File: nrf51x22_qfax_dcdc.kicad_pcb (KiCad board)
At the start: 2 copper layers, 14.8 x 16.4 mm, 45 parts, among them U1 nrf51822-qfax, X1 Crystal, X2 XTAL SMD 3.2 x 1.5 mm

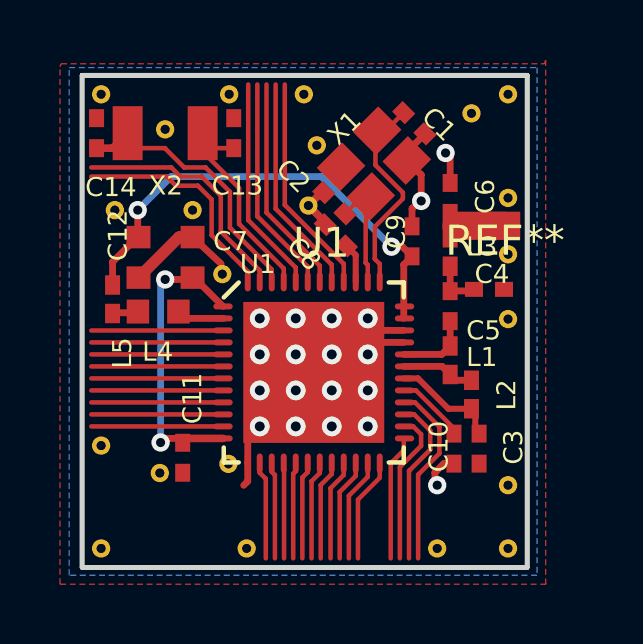
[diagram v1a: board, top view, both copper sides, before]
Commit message: missed replacing a via
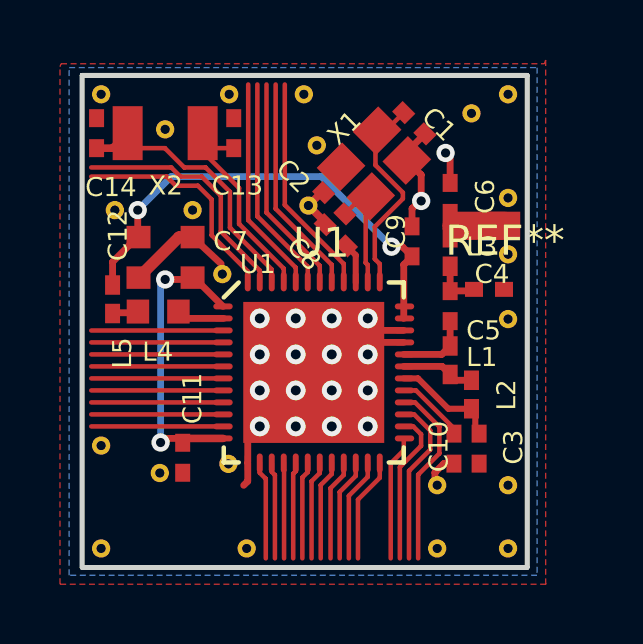
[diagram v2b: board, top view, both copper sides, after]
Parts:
- added REF**: VIA-0.6096, dcdc:VIA-0.6096, F.Cu at (88.2, -81.7)
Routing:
- net GND: vias 19 -> 18
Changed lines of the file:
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@@
 (kicad_pcb (version 4) (host pcbnew 4.0.0-stable)
   (general
-    (links 65)
+    (links 67)
     (no_connects 3)
-    (area 76.307339 -95.473821 91.295321 -78.913019)
+    (area 41.129536 -98.38002 117.176334 -76.15682)
     (thickness 1.6)
     (drawings 30)
-    (tracks 217)
+    (tracks 216)
     (zones 0)
-    (modules 45)
+    (modules 46)
     (nets 50)
   )
@@
   (layers
     (0 F.Cu signal)
-    (31 B.Cu signal hide)
+    (31 B.Cu signal)
     (32 B.Adhes user)
     (33 F.Adhes user)
@@
     )
   )
+  (module dcdc:VIA-0.6096 (layer F.Cu)
+    (at 88.22073 -81.73242)
+    (fp_text reference REF** (at 0 2.54) (layer F.SilkS) hide
+      (effects (font (size 1 1) (thickness 0.15)))
+    )
+    (fp_text value VIA-0.6096 (at 0 -2.54) (layer F.Fab) hide
+      (effects (font (size 1 1) (thickness 0.15)))
+    )
+    (pad 1 thru_hole circle (at 0 0) (size 0.6096 0.6096) (drill 0.3048) (layers *.Cu)
+      (zone_connect 2))
+  )
   (gr_line (start 76.38354 -78.98922) (end 76.38354 -95.39762) (layer Edge.Cuts) (width 0.1524))
   (gr_line (start 76.38354 -78.98922) (end 91.21912 -78.98922) (layer Edge.Cuts) (width 0.1524))
@@
   (segment (start 81.61673 -90.44313) (end 81.61673 -91.63842) (width 0.1524) (layer F.Cu) (net 2))
   (segment (start 81.61673 -90.44313) (end 83.10593 -88.95392) (width 0.1524) (layer F.Cu) (net 2))
-  (via (at 88.22073 -81.73242) (size 0.6096) (drill 0.3048) (layers F.Cu B.Cu) (net 3))
   (segment (start 88.14453 -81.88482) (end 88.14453 -82.15573) (width 0.2286) (layer F.Cu) (net 3))
   (segment (start 88.14453 -82.15573) (end 88.44042 -82.45162) (width 0.2286) (layer F.Cu) (net 3))

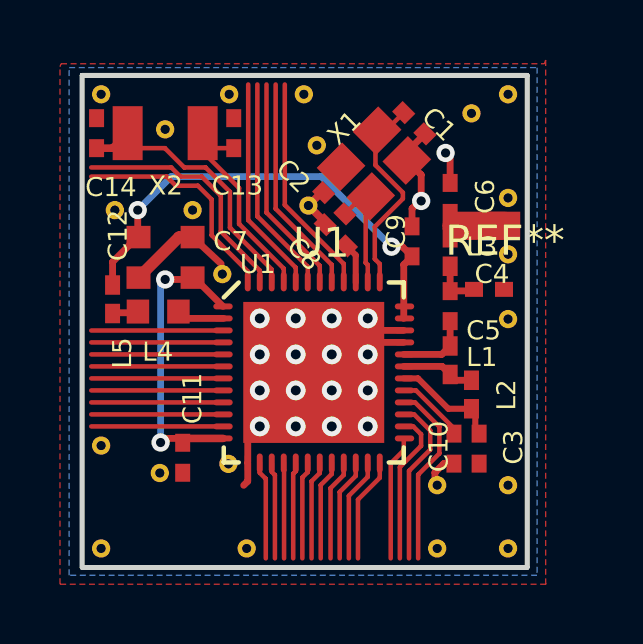
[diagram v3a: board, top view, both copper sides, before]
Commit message: add vias to footprint and swap in
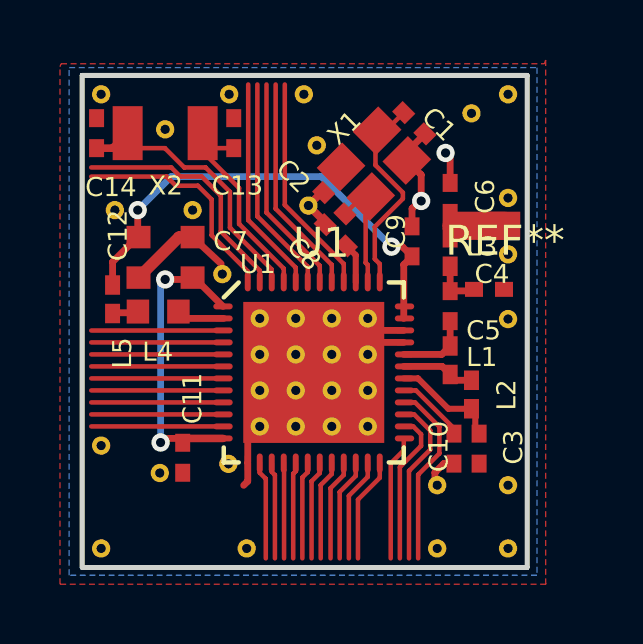
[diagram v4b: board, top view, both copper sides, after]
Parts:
- U1: footprint nrf:nrf51-qfax -> nrf:nrf51-qfax-1ep-vias
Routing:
- net GND: vias 18 -> 2

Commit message: merge library update
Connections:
- U1 pad 10: Net-(U1-Pad10) -> (no net)
- U1 pad 11: Net-(U1-Pad11) -> (no net)
- U1 pad 14: Net-(U1-Pad14) -> (no net)
- U1 pad 15: Net-(U1-Pad15) -> (no net)
- U1 pad 16: Net-(U1-Pad16) -> (no net)
- U1 pad 17: Net-(U1-Pad17) -> (no net)
- U1 pad 18: Net-(U1-Pad18) -> (no net)
- U1 pad 19: Net-(U1-Pad19) -> (no net)
- U1 pad 20: Net-(U1-Pad20) -> (no net)
- U1 pad 21: Net-(U1-Pad21) -> (no net)
- U1 pad 22: Net-(U1-Pad22) -> (no net)
- U1 pad 23: Net-(U1-Pad23) -> (no net)
- U1 pad 24: Net-(U1-Pad24) -> (no net)
- U1 pad 25: Net-(U1-Pad25) -> (no net)
- U1 pad 26: Net-(U1-Pad26) -> (no net)
- U1 pad 27: Net-(U1-Pad27) -> (no net)
- U1 pad 28: Net-(U1-Pad28) -> (no net)
- U1 pad 3: Net-(U1-Pad3) -> (no net)
- U1 pad 4: Net-(U1-Pad4) -> (no net)
- U1 pad 40: Net-(U1-Pad40) -> (no net)
- U1 pad 41: Net-(U1-Pad41) -> (no net)
- U1 pad 42: Net-(U1-Pad42) -> (no net)
- U1 pad 43: Net-(U1-Pad43) -> (no net)
- U1 pad 44: Net-(U1-Pad44) -> (no net)
- U1 pad 45: Net-(U1-Pad45) -> (no net)
- U1 pad 46: Net-(U1-Pad46) -> (no net)
- U1 pad 47: Net-(U1-Pad47) -> (no net)
- U1 pad 48: Net-(U1-Pad48) -> (no net)
- U1 pad 5: Net-(U1-Pad5) -> (no net)
- U1 pad 6: Net-(U1-Pad6) -> (no net)
- U1 pad 7: Net-(U1-Pad7) -> (no net)
- U1 pad 8: Net-(U1-Pad8) -> (no net)
- U1 pad 9: Net-(U1-Pad9) -> (no net)
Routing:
- net (no net): track 0.00 -> 149.8 mm
- net Net-(U1-Pad47): track 8.14 -> 0.00 mm
- net Net-(U1-Pad48): track 7.59 -> 0.00 mm
- net Net-(U1-Pad40): track 7.41 -> 0.00 mm
- net Net-(U1-Pad41): track 7.37 -> 0.00 mm
- net Net-(U1-Pad42): track 7.33 -> 0.00 mm
- net Net-(U1-Pad43): track 7.29 -> 0.00 mm
- net Net-(U1-Pad44): track 7.26 -> 0.00 mm
- net Net-(U1-Pad28): track 6.20 -> 0.00 mm
- net Net-(U1-Pad27): track 5.66 -> 0.00 mm
- net Net-(U1-Pad26): track 5.12 -> 0.00 mm
- net Net-(U1-Pad9): track 4.42 -> 0.00 mm
- net Net-(U1-Pad8): track 4.42 -> 0.00 mm
- net Net-(U1-Pad7): track 4.42 -> 0.00 mm
- net Net-(U1-Pad6): track 4.42 -> 0.00 mm
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
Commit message: fix crystal component so hooks grounds to GND, gerbers
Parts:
- X1: value Crystal -> Crystal-4
- turned C1 to 315 degrees
- turned C10 to 90 degrees
- turned C11 to 270 degrees
- turned C13 to 270 degrees
- turned C14 to 270 degrees
- turned C2 to 135 degrees
- turned C3 to 270 degrees
- turned C4 to 0 degrees
- turned C5 to 270 degrees
- turned C6 to 90 degrees
- turned C8 to 315 degrees
- turned C9 to 90 degrees
- turned L1 to 0 degrees
- turned L2 to 0 degrees
- turned L3 to 180 degrees
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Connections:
- X1 pad 2: Net-(C1-Pad1) -> GND
- X1 pad 3: GND -> Net-(C1-Pad1)

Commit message: fix missing low freq crystal on schematic
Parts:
- C13, C14: value Chip Capacitor, 2-Leads, Body 1.0x0.5mm, IPC High Density -> 12pF
- X2: value XTAL SMD 3.2 x 1.5 mm -> 32.768kHz
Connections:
- C13 pad 2: XL2 -> Net-(C13-Pad2)
- C14 pad 2: XL1 -> Net-(C14-Pad2)
- U1 pad 45: (no net) -> Net-(C13-Pad2)
- U1 pad 46: (no net) -> Net-(C14-Pad2)
- X2 pad 1: XL2 -> Net-(C13-Pad2)
- X2 pad 2: XL1 -> Net-(C14-Pad2)
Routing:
- net XL1: track 9.89 -> 0.00 mm
- net Net-(C14-Pad2): track 0.00 -> 9.89 mm
- net XL2: track 6.04 -> 0.00 mm
- net Net-(C13-Pad2): track 0.00 -> 6.04 mm
